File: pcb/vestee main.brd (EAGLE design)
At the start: 65 x 65 mm, 47 parts, among them IC1 LD117AS12TR, IC2 FT232RL, Q1 MMBT2222A, Q2 MMBT5088, Q3 MMBT4403, Q4 MMBT5088

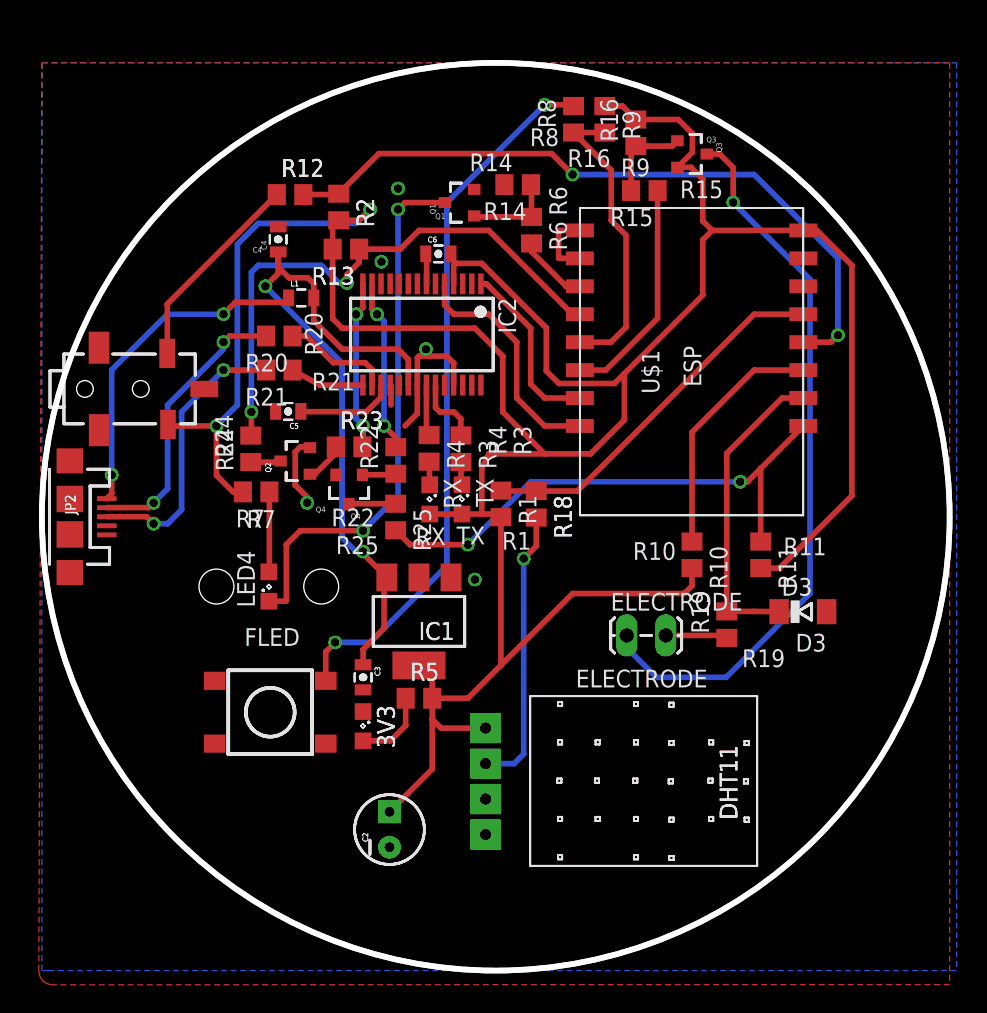
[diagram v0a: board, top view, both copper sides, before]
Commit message: Added new LED to GPIO12, screw holes, bottom layer fixes
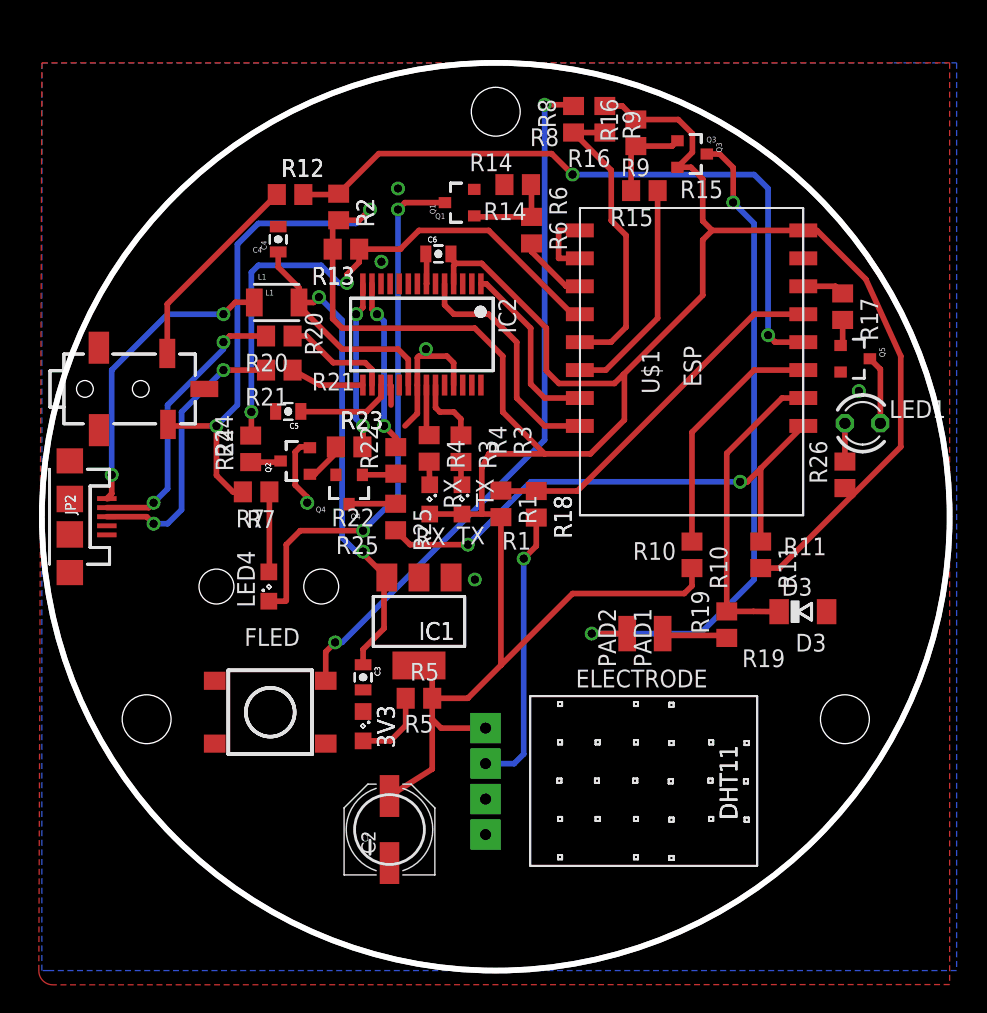
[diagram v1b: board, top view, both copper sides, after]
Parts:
- removed ELECTRODE: (no value), SparkFun-Connectors:1X02_LOCK_LONGPADS
- added LED1: (no value), led:LED3MM
- added PAD1, PAD2: (no value), wirepad:SMD1,27-2,54
- added Q5: MMBT5088, SparkFun-DiscreteSemi:SOT23-3
- added R17, R26: (no value), rcl:R0805
- C2: device SparkFun-Capacitors:CPOL-RADIAL-10UF-25V -> SparkFun-Capacitors:PANASONIC_D
- L1: device SparkFun-Passives:0805 -> SparkFun-Passives:1210
- moved L1 1.79 mm to (16.8, 47.8)
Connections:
- new net N$20: R17.1, U$1.GPIO12
- new net N$22: LED1.K, Q5.3
- new net N$23: LED1.A, R26.2
- new net N$5: Q5.1, R17.2
- net GND: now also C2.-, Q5.2; no longer C2.2
- net N$17: now also PAD2.1; no longer ELECTRODE.1
- net N$26: now also PAD1.1; no longer ELECTRODE.2
- net VCC: now also C2.+, R26.1; no longer C2.1
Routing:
- net N$22: track 0.00 -> 4.93 mm
- net VIN: track 51.1 -> 46.7 mm
- net N$17: track 52.4 -> 48.2 mm, vias 1 -> 2
- net N$20: track 0.00 -> 3.03 mm
- net N$23: track 0.00 -> 2.74 mm
- net N$7: track 24.3 -> 21.7 mm
- net VCC: track 224.1 -> 226.6 mm
- net N$4: track 50.8 -> 48.8 mm
- net N$5: track 0.00 -> 1.89 mm
- net N$18: track 51.3 -> 50.1 mm
- net GND: vias 5 -> 6
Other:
- board text added: "and"
- board text added: "vestee.io"
- board text removed: "vestee for Monterail"

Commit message: Moved button to the center
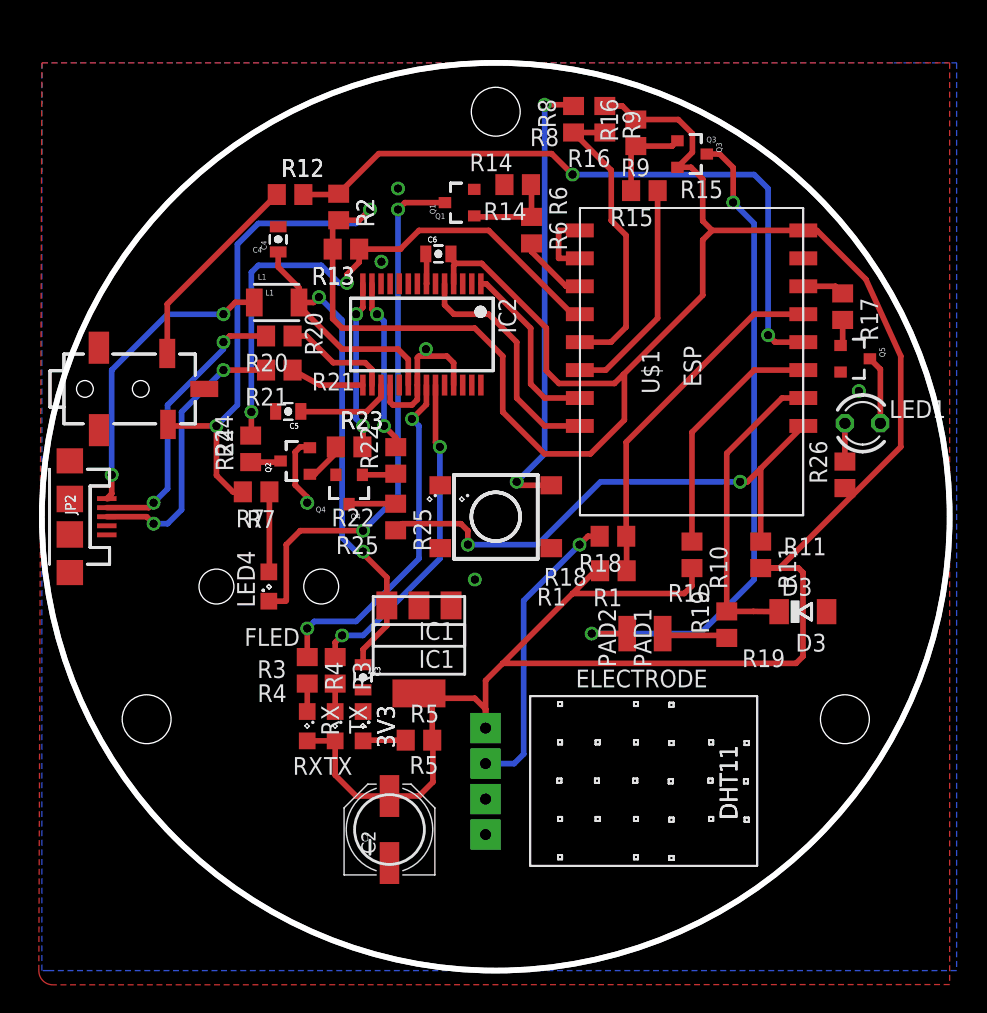
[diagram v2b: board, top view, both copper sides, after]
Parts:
- moved S2 21.4 mm to (32.5, 32.5)
- moved TX 18.6 mm to (21.0, 17.5)
- moved RX 18.5 mm to (19.0, 17.5)
- moved R3 18.2 mm to (21.0, 21.5)
- moved R4 18.1 mm to (19.0, 21.5)
- moved R1 9.37 mm to (40.9, 28.6), turned to 180 degrees
- moved R18 5.95 mm to (40.9, 31.1), turned to 180 degrees
- moved R5 3.00 mm to (27.0, 16.5)
- moved IC1 2.00 mm to (27.0, 23.0)
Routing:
- net N$12: track 3.67 -> 25.2 mm, vias 0 -> 2
- net VCC: track 226.6 -> 245.3 mm
- net N$11: track 4.95 -> 23.6 mm, vias 0 -> 2
- net N$18: track 50.1 -> 32.5 mm
- net N$8: track 5.46 -> 3.07 mm
- net N$1: track 26.9 -> 25.7 mm
- net N$6: track 20.3 -> 21.4 mm
- net CBUS_RST: track 38.4 -> 39.3 mm

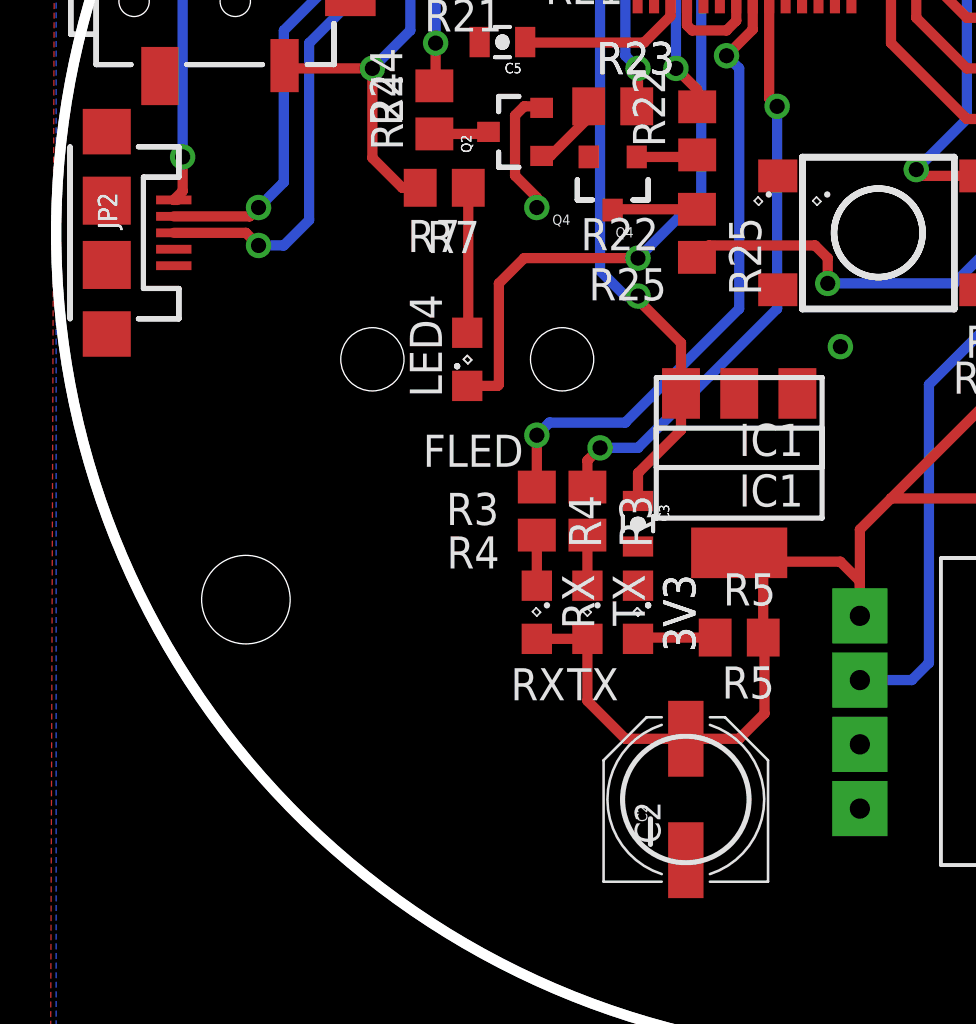
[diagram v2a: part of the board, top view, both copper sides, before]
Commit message: Add VCC pads, move silk
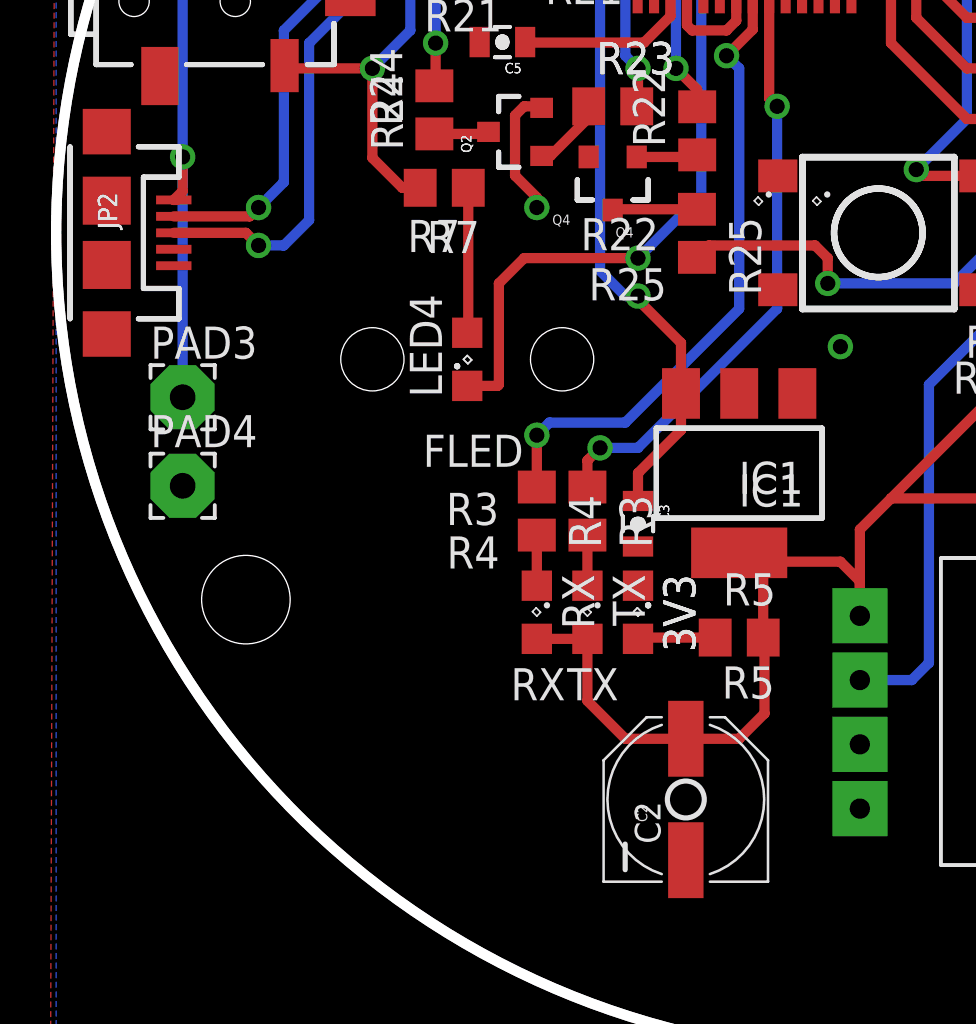
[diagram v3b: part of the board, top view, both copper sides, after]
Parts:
- added PAD3, PAD4: WIREPAD2,54/1,0, wirepad:2,54/1,0
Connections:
- net GND: now also PAD4.1
- net N$7: now also PAD3.1
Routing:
- net N$7: track 21.7 -> 31.2 mm
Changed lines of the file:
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@@
 <?xml version="1.0" encoding="utf-8"?>
 <!DOCTYPE eagle SYSTEM "eagle.dtd">
-<eagle version="7.4.0">
+<eagle version="7.1.0">
 <drawing>
 <settings>
@@
 <layer number="19" name="Unrouted" color="14" fill="1" visible="yes" active="yes"/>
 <layer number="20" name="Dimension" color="15" fill="1" visible="yes" active="yes"/>
-<layer number="21" name="tPlace" color="7" fill="1" visible="no" active="yes"/>
+<layer number="21" name="tPlace" color="7" fill="1" visible="yes" active="yes"/>
 <layer number="22" name="bPlace" color="7" fill="1" visible="yes" active="yes"/>
-<layer number="23" name="tOrigins" color="15" fill="1" visible="no" active="yes"/>
+<layer number="23" name="tOrigins" color="15" fill="1" visible="yes" active="yes"/>
 <layer number="24" name="bOrigins" color="15" fill="1" visible="yes" active="yes"/>
-<layer number="25" name="tNames" color="7" fill="1" visible="no" active="yes"/>
+<layer number="25" name="tNames" color="7" fill="1" visible="yes" active="yes"/>
 <layer number="26" name="bNames" color="7" fill="1" visible="yes" active="yes"/>
-<layer number="27" name="tValues" color="7" fill="1" visible="no" active="yes"/>
+<layer number="27" name="tValues" color="7" fill="1" visible="yes" active="yes"/>
 <layer number="28" name="bValues" color="7" fill="1" visible="yes" active="yes"/>
 <layer number="29" name="tStop" color="7" fill="3" visible="yes" active="yes"/>
@@
 <circle x="23.400003125" y="17.774996875" radius="0.12499375" width="0" layer="121"/>
 <text x="24.000003125" y="18.9999875" size="1.27" layer="121" font="vector" rot="R270">3V3</text>
-<wire x1="23.49299375" y1="9.33800625" x2="23.49299375" y2="8.32200625" width="0.2032" layer="121"/>
-<circle x="24.88999375" y="10.10000625" radius="2.49999375" width="0.2032" layer="121"/>
+<wire x1="22.49299375" y1="8.33800625" x2="22.49299375" y2="7.32200625" width="0.2032" layer="121"/>
+<circle x="24.88999375" y="10.10000625" radius="0.729453125" width="0.2032" layer="121"/>
 <text x="23.36599375" y="9.21100625" size="0.4064" layer="121" font="vector" rot="R90">C2</text>
 <wire x1="23.600003125" y1="21.300009375" x2="23.600003125" y2="20.700009375" width="0.1524" layer="121"/>
@@
 <text x="53.966009375" y="22.843" size="1.27" layer="121" font="vector">D3</text>
 <text x="38.22999375" y="20.278003125" size="1.27" layer="121" font="vector">ELECTRODE</text>
-<wire x1="23.722990625" y1="23.222" x2="23.722990625" y2="26.778" width="0.2032" layer="121"/>
-<wire x1="23.722990625" y1="26.778" x2="30.277003125" y2="26.778" width="0.2032" layer="121"/>
-<wire x1="30.277003125" y1="26.778" x2="30.277003125" y2="23.222" width="0.2032" layer="121"/>
-<wire x1="30.277003125" y1="23.222" x2="23.722990625" y2="23.222" width="0.2032" layer="121"/>
-<text x="29.539996875" y="24.9492" size="1.27" layer="121" font="vector" rot="R180">IC1</text>
+<wire x1="23.722990625" y1="21.222" x2="23.722990625" y2="24.778" width="0.2032" layer="121"/>
+<wire x1="23.722990625" y1="24.778" x2="30.277003125" y2="24.778" width="0.2032" layer="121"/>
+<wire x1="30.277003125" y1="24.778" x2="30.277003125" y2="21.222" width="0.2032" layer="121"/>
+<wire x1="30.277003125" y1="21.222" x2="23.722990625" y2="21.222" width="0.2032" layer="121"/>
+<text x="29.539996875" y="23.4492" size="1.27" layer="121" font="vector" rot="R180">IC1</text>
 <wire x1="32.30999375" y1="48.14999375" x2="22.1099875" y2="48.14999375" width="0.2032" layer="121"/>
 <wire x1="22.1099875" y1="48.14999375" x2="22.1099875" y2="42.950003125" width="0.2032" layer="121"/>
@@
 <element name="R17" library="rcl" package="R0805" value="" x="57.34" y="47.54" rot="R270"/>
 <element name="R26" library="rcl" package="R0805" value="" x="57.5" y="35.5" rot="R90"/>
+<element name="PAD3" library="wirepad" package="2,54/1,0" value="WIREPAD2,54/1,0" x="5" y="26"/>
+<element name="PAD4" library="wirepad" package="2,54/1,0" value="WIREPAD2,54/1,0" x="5" y="22.5"/>
 </elements>
 <signals>
@@
 <wire x1="25.14" y1="40.5" x2="24.935" y2="40.705" width="0.4064" layer="1"/>
 <wire x1="24.935" y1="40.705" x2="24.935" y2="41.925" width="0.4064" layer="1"/>
+<contactref element="PAD4" pad="1"/>
 </signal>
 <signal name="VCC">
@@
 <wire x1="13.8567" y1="47.8567" x2="15.1933" y2="47.8567" width="0.4064" layer="1"/>
 <wire x1="15.1933" y1="47.8567" x2="15.21" y2="47.84" width="0.4064" layer="1"/>
+<contactref element="PAD3" pad="1"/>
+<wire x1="5" y1="26" x2="5" y2="35.5" width="0.4064" layer="16"/>
 </signal>
 <signal name="N$9">

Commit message: Version 2, all issues fixed
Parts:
- removed 3V3, RX, TX: (no value), led:SML0805
- removed LED1: (no value), led:LED3MM
- removed PAD3, PAD4: WIREPAD2,54/1,0, wirepad:2,54/1,0
- removed Q2, Q4, Q5: MMBT5088, SparkFun-DiscreteSemi:SOT23-3
- removed R13, R17, R22, R23, R24, R25, R26, R4, R5: (no value), rcl:R0805
- added DBG_TX, DBG_TX1, PAD5: (no value), wirepad:SMD1,27-2,54
- PRPIHERALS: value (none) -> AUDIO-JACK-2.5-CUI; device SparkFun-Connectors:STEREOJACK2.5MM -> SparkFun-Connectors:STEREOJACK2.5_SMD_CUI
- moved Q3 44.1 mm to (49.4, 14.5), turned to 180 degrees
- moved R9 42.9 mm to (46.5, 18.5), turned to 90 degrees
- moved R8 42.9 mm to (43.5, 18.4), turned to 270 degrees
- moved R16 42.1 mm to (49.5, 18.4)
- moved R15 38.5 mm to (52.5, 18.4), turned to 270 degrees
- moved D3 27.3 mm to (52.8, 53.0), turned to 90 degrees
- moved R19 23.5 mm to (50.2, 48.2), turned to 270 degrees
- moved C2 21.9 mm to (8.89, 25.1)
- moved R3 19.7 mm to (40.5, 18.5), turned to 90 degrees
- moved R1 19.6 mm to (40.3, 48.2), turned to 270 degrees
- moved R11 18.8 mm to (55.2, 48.2), turned to 90 degrees
- moved R10 18.5 mm to (47.7, 48.2), turned to 90 degrees
- moved R18 17.7 mm to (45.3, 48.2), turned to 90 degrees
- moved LED4 16.7 mm to (32.5, 23.7), turned to 270 degrees
- moved PAD2 16.6 mm to (50.9, 10.1)
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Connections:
- removed net CBUS: R13.1, R24.2, U$1.GPIO0
- removed net CBUS_RST: R11.1, R25.2, U$1.REST
- removed net N$11: IC2.23, R3.1
- removed net N$12: IC2.22, R4.1
- removed net N$13: R3.2, TX.C
- removed net N$14: R4.2, RX.C
- removed net N$20: R17.1, U$1.GPIO12
- removed net N$22: LED1.K, Q5.3
- removed net N$23: LED1.A, R26.2
- removed net N$30: IC2.13, R22.2
- removed net N$31: Q2.3, R24.1
- removed net N$32: Q2.1, R23.1
- removed net N$33: Q4.1, R22.1
- removed net N$34: IC2.14, R23.2
- removed net N$35: Q4.3, R25.1
- removed net N$8: 3V3.A, R5.1
- new net DTR: IC2.2, R3.2, U$1.GPIO0
- new net RTS: IC2.3, R11.1, U$1.REST
- net 1-WIRE: now also PRPIHERALS.3; no longer PRPIHERALS.1
- net FLED: now also U$1.GPIO12; no longer U$1.GPIO2
- net GND: now also DBG_TX1.1, PAD5.1, PRPIHERALS.1; no longer 3V3.C, PAD4.1, PRPIHERALS.5, Q2.2, Q4.2, Q5.2
- net N$5: now also DBG_TX.1, U$1.GPIO2; no longer Q5.1, R17.2
- net N$7: no longer PAD3.1
- net VCC: now also PRPIHERALS.2, R3.1; no longer PRPIHERALS.4, R13.2, R26.1, R5.2, RX.A, TX.A
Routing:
- net VCC: track 245.3 -> 182.1 mm, vias 2 -> 4
- net N$6: track 21.4 -> 70.4 mm, vias 1 -> 2
- net N$17: track 48.2 -> 3.89 mm, vias 2 -> 0
- net N$26: track 4.72 -> 46.1 mm, vias 0 -> 2
- net DTR: track 0.00 -> 41.2 mm
- net CBUS: track 40.9 -> 0.00 mm, vias 2 -> 0
- net CBUS_RST: track 39.3 -> 0.00 mm, vias 2 -> 0
- net RTS: track 0.00 -> 31.8 mm
- net N$12: track 25.2 -> 0.00 mm, vias 2 -> 0
- net N$11: track 23.6 -> 0.00 mm, vias 2 -> 0
- net N$15: track 5.75 -> 23.4 mm
- net N$28: track 5.31 -> 20.9 mm, vias 0 -> 2
- net N$7: track 31.2 -> 15.9 mm, vias 2 -> 0
- net FTDI_TXD: track 12.8 -> 26.5 mm
- net FTDI_RXD: track 17.1 -> 30.2 mm, vias 0 -> 2
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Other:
- board text removed: "/Users/grzegorz/Documents/montebmp.bmp"
- board text removed: "3V3"
- board text removed: "C2"
- board text removed: "C3"
- board text removed: "C4"
- board text removed: "C5"
- board text removed: "C6"
- board text removed: "D3"
- board text removed: "DHT11"
- board text removed: "ELECTRODE"
- board text removed: "ESP"
- board text removed: "FLED"
- board text removed: "IC1"
- board text removed: "JP2"
- board text removed: "L1"
- board text removed: "Q1"
- board text removed: "Q2"
- board text removed: "Q3"
- board text removed: "Q4"
- board text removed: "R1"
- board text removed: "R10"
- board text removed: "R11"
- board text removed: "R12"
- board text removed: "R13"
- board text removed: "R14"
- board text removed: "R15"
- board text removed: "R16"
- board text removed: "R18"
- board text removed: "R19"
- board text removed: "R2"
- board text removed: "R20"
- board text removed: "R21"
- board text removed: "R22"
- board text removed: "R23"
- board text removed: "R24"
- board text removed: "R25"
- board text removed: "R3"
- board text removed: "R4"
- board text removed: "R5"
- board text removed: "R6"
- board text removed: "R7"
- board text removed: "R8"
- board text removed: "R9"
- board text removed: "RX"
- board text removed: "TX"
- board text removed: "vestee"
